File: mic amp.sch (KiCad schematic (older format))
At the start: 32 parts, among them J1 CONN_01X02, J10 CONN_01X02, J2 CONN_01X01, J3 CONN_01X03, J4 CONN_01X01, J5 CONN_01X01, J6 CONN_01X01, J7 CONN_01X01, J8 CONN_01X02, J9 CONN_01X03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

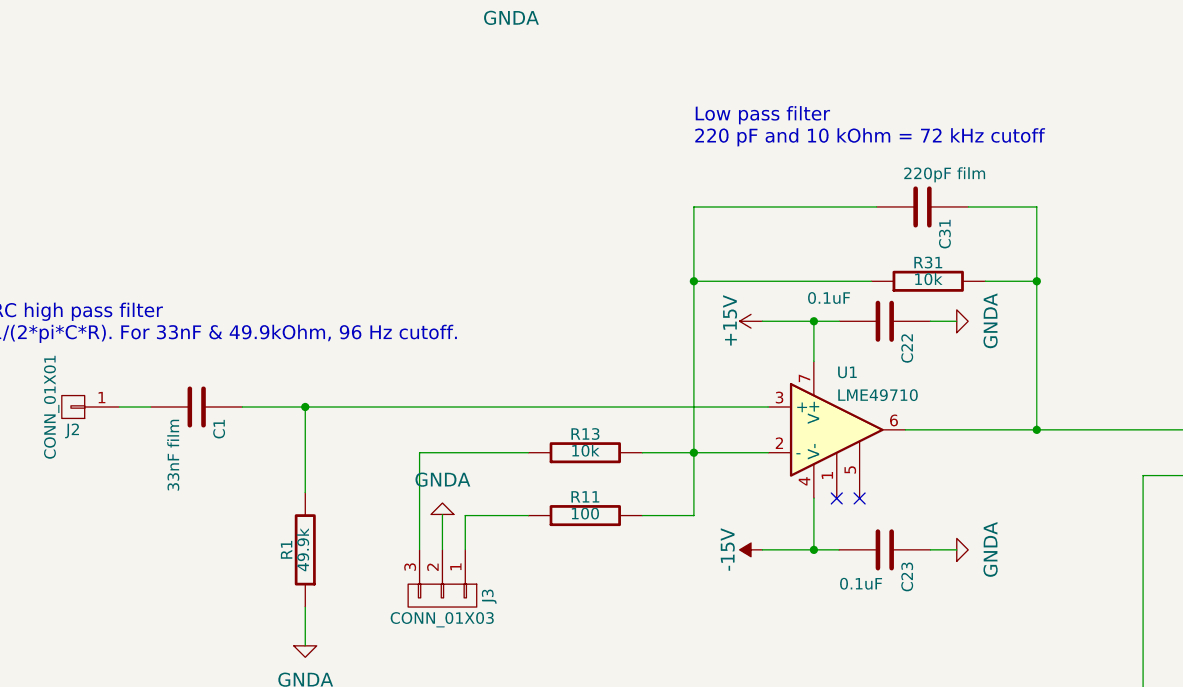
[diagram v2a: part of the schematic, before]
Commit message: Update readme and added parts list and PCB image
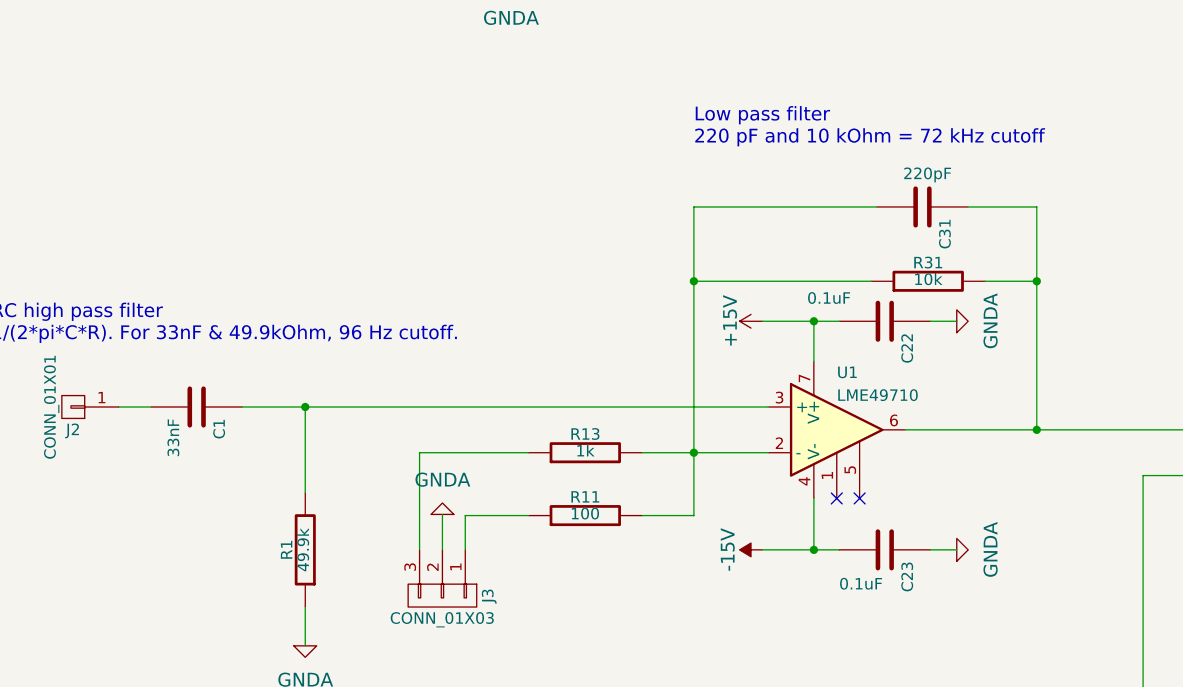
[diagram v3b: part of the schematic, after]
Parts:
- C1: value 33nF film -> 33nF; Notes (none) -> use metal film; Part number (none) -> FKP2C023301L00HI00
- C10, C11: Part number (none) -> RDER72A105K2P1H03B
- C12, C13, C22, C23, C5: Part number (none) -> RDER72A104K1S1H03A
- C31: value 220pF film -> 220pF; Notes (none) -> use metal film; Part number (none) -> FKP2D002201D00HSSD
- C6, C7: Part number (none) -> UKL1V101KPDANA
- R1: Part number (none) -> YR1B49K9CC
- R10, R11: Part number (none) -> YR1B100RCC
- R13: value 10k -> 1k; Part number (none) -> YR1B1K0CC
- R22: Part number (none) -> YR1B499RCC
- R23: Part number (none) -> YR1B90R9CC
- R24: Part number (none) -> YR1B4K75CC
- R31: Part number (none) -> YR1B10KCC
- U1: Notes (none) -> this part is end-of-life, order extra if you need more; Part number (none) -> LME49710NA/NOPB
- U2: Part number (none) -> LF356N/NOPB
- VREG1: Part number (none) -> LM317LZ/NOPB
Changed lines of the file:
@@
 F 2 "Package_TO_SOT_THT:TO-92_Inline_Wide" H 3775 1425 60  0001 C CNN
 F 3 "" H 3775 1425 60  0000 C CNN
+F 4 "LM317LZ/NOPB" H 3775 1425 60  0001 C CNN "Part number"
 	1    3775 1425
 	-1   0    0    -1
@@
 F 2 "Resistor_THT:R_Axial_DIN0207_L6.3mm_D2.5mm_P7.62mm_Horizontal" V 3705 2450 30  0001 C CNN
 F 3 "" H 3775 2450 30  0000 C CNN
+F 4 "YR1B90R9CC" H 3775 2450 60  0001 C CNN "Part number"
 	1    3775 2450
 	1    0    0    -1
@@
 F 2 "Resistor_THT:R_Axial_DIN0207_L6.3mm_D2.5mm_P7.62mm_Horizontal" V 3230 2000 30  0001 C CNN
 F 3 "" H 3300 2000 30  0000 C CNN
+F 4 "YR1B499RCC" H 3300 2000 60  0001 C CNN "Part number"
 	1    3300 2000
 	0    1    1    0
@@
 F 2 "Resistor_THT:R_Axial_DIN0207_L6.3mm_D2.5mm_P7.62mm_Horizontal" V 2405 2000 30  0001 C CNN
 F 3 "" H 2475 2000 30  0000 C CNN
+F 4 "YR1B4K75CC" H 2475 2000 60  0001 C CNN "Part number"
 	1    2475 2000
 	0    1    1    0
@@
 F 2 "custom:C_Rect_L4.0mm_W3.5mm_P2.50mm" H 4488 1875 30  0001 C CNN
 F 3 "" H 4450 2025 60  0000 C CNN
+F 4 "RDER72A104K1S1H03A" H 4450 2025 60  0001 C CNN "Part number"
 	1    4450 2025
 	1    0    0    -1
@@
 F 2 "Capacitor_THT:CP_Radial_D10.0mm_P5.00mm" H 2938 2300 30  0001 C CNN
 F 3 "" H 2900 2450 60  0000 C CNN
+F 4 "UKL1V101KPDANA" H 2900 2450 60  0001 C CNN "Part number"
 	1    2900 2450
 	1    0    0    -1
@@
 F 2 "Capacitor_THT:CP_Radial_D10.0mm_P5.00mm" H 2088 2300 30  0001 C CNN
 F 3 "" H 2050 2450 60  0000 C CNN
+F 4 "UKL1V101KPDANA" H 2050 2450 60  0001 C CNN "Part number"
 	1    2050 2450
 	1    0    0    -1
@@
 F 2 "Resistor_THT:R_Axial_DIN0207_L6.3mm_D2.5mm_P7.62mm_Horizontal" V 2380 5675 30  0001 C CNN
 F 3 "" H 2450 5675 30  0000 C CNN
+F 4 "YR1B49K9CC" H 2450 5675 60  0001 C CNN "Part number"
 	1    2450 5675
 	-1   0    0    1
@@
 P 1975 5050
 F 0 "C1" H 2025 5150 50  0000 L CNN
-F 1 "33nF film" H 2025 4950 50  0000 L CNN
+F 1 "33nF" H 2025 4950 50  0000 L CNN
 F 2 "Capacitor_THT:C_Rect_L7.2mm_W8.5mm_P5.00mm_FKP2_FKP2_MKS2_MKP2" H 2013 4900 30  0001 C CNN
 F 3 "" H 1975 5050 60  0000 C CNN
+F 4 "FKP2C023301L00HI00" H 1975 5050 60  0001 C CNN "Part number"
+F 5 "use metal film" H 1975 5050 60  0001 C CNN "Notes"
 	1    1975 5050
 	0    1    1    0
@@
 P 3675 5250
 F 0 "R13" V 3755 5250 50  0000 C CNN
-F 1 "10k" V 3682 5251 50  0000 C CNN
+F 1 "1k" V 3682 5251 50  0000 C CNN
 F 2 "Resistor_THT:R_Axial_DIN0207_L6.3mm_D2.5mm_P7.62mm_Horizontal" V 3605 5250 30  0001 C CNN
 F 3 "" H 3675 5250 30  0000 C CNN
+F 4 "YR1B1K0CC" H 3675 5250 60  0001 C CNN "Part number"
 	1    3675 5250
 	0    -1   -1   0
@@
 F 2 "Resistor_THT:R_Axial_DIN0207_L6.3mm_D2.5mm_P7.62mm_Horizontal" V 3605 5525 30  0001 C CNN
 F 3 "" H 3675 5525 30  0000 C CNN
+F 4 "YR1B100RCC" H 3675 5525 60  0001 C CNN "Part number"
 	1    3675 5525
 	0    -1   -1   0
@@
 F 2 "Resistor_THT:R_Axial_DIN0207_L6.3mm_D2.5mm_P7.62mm_Horizontal" V 5105 4500 30  0001 C CNN
 F 3 "" H 5175 4500 30  0000 C CNN
+F 4 "YR1B10KCC" H 5175 4500 60  0001 C CNN "Part number"
 	1    5175 4500
 	0    -1   -1   0
@@
 P 5150 4175
 F 0 "C31" H 5200 4275 50  0000 L CNN
-F 1 "220pF film" V 5005 4090 50  0000 L CNN
+F 1 "220pF" V 5005 4090 50  0000 L CNN
 F 2 "Capacitor_THT:C_Rect_L7.2mm_W4.5mm_P5.00mm_FKS2_FKP2_MKS2_MKP2" H 5188 4025 30  0001 C CNN
 F 3 "" H 5150 4175 60  0000 C CNN
+F 4 "FKP2D002201D00HSSD" H 5150 4175 60  0001 C CNN "Part number"
+F 5 "use metal film" H 5150 4175 60  0001 C CNN "Notes"
 	1    5150 4175
 	0    1    1    0
@@
 F 2 "custom:C_Rect_L4.0mm_W3.5mm_P2.50mm" H 7088 4600 30  0001 C CNN
 F 3 "" H 7050 4750 60  0000 C CNN
+F 4 "RDER72A104K1S1H03A" H 7050 4750 60  0001 C CNN "Part number"
 	1    7050 4750
 	0    1    1    0
@@
 F 2 "custom:C_Rect_L4.0mm_W3.5mm_P2.50mm" H 7088 5600 30  0001 C CNN
 F 3 "" H 7050 5750 60  0000 C CNN
+F 4 "RDER72A104K1S1H03A" H 7050 5750 60  0001 C CNN "Part number"
 	1    7050 5750
 	0    1    1    0
@@
 F 2 "Resistor_THT:R_Axial_DIN0207_L6.3mm_D2.5mm_P7.62mm_Horizontal" V 7730 5250 30  0001 C CNN
 F 3 "" H 7800 5250 30  0000 C CNN
+F 4 "YR1B100RCC" H 7800 5250 60  0001 C CNN "Part number"
 	1    7800 5250
 	0    -1   -1   0
@@
 F 2 "custom:C_Rect_L5.5mm_W4.0mm_P2.50mm" H 6418 2300 30  0001 C CNN
 F 3 "" H 6380 2450 60  0000 C CNN
+F 4 "RDER72A105K2P1H03B" H 6380 2450 60  0001 C CNN "Part number"
 	1    6380 2450
 	1    0    0    -1
@@
 F 2 "custom:C_Rect_L5.5mm_W4.0mm_P2.50mm" H 6088 2300 30  0001 C CNN
 F 3 "" H 6050 2450 60  0000 C CNN
+F 4 "RDER72A105K2P1H03B" H 6050 2450 60  0001 C CNN "Part number"
 	1    6050 2450
 	1    0    0    -1
@@
 F 2 "custom:C_Rect_L4.0mm_W3.5mm_P2.50mm" H 5023 4525 30  0001 C CNN
 F 3 "" H 4985 4675 60  0000 C CNN
+F 4 "RDER72A104K1S1H03A" H 4985 4675 60  0001 C CNN "Part number"
 	1    4985 4675
 	0    1    1    0
@@
 F 2 "custom:C_Rect_L4.0mm_W3.5mm_P2.50mm" H 5023 5525 30  0001 C CNN
 F 3 "" H 4985 5675 60  0000 C CNN
+F 4 "RDER72A104K1S1H03A" H 4985 5675 60  0001 C CNN "Part number"
 	1    4985 5675
 	0    1    1    0
@@
 F 2 "Package_DIP:DIP-8_W7.62mm_LongPads" H 6745 5300 50  0001 C CNN
 F 3 "" H 6845 5400 50  0001 C CNN
+F 4 "LF356N/NOPB" H 6695 5250 60  0001 C CNN "Part number"
 	1    6695 5250
 	1    0    0    -1
@@
 F 2 "Package_DIP:DIP-8_W7.62mm_LongPads" H 4825 5200 50  0001 C CNN
 F 3 "" H 4925 5300 50  0001 C CNN
+F 4 "LME49710NA/NOPB" H 4775 5150 60  0001 C CNN "Part number"
+F 5 "this part is end-of-life, order extra if you need more" H 4775 5150 60  0001 C CNN "Notes"
 	1    4775 5150
 	1    0    0    -1

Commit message: Update parts list, fix circuit board image
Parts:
- J1, J10, J2, J3, J8, J9: Notes (none) -> 0.1\" header
- J4, J5, J6, J7: Notes (none) -> mounting hole
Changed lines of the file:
@@
 F 2 "Conn_PinSocket_2.54mm:PinSocket_1x03_P2.54mm_Vertical" H 3050 5875 50  0001 C CNN
 F 3 "" H 3050 5875 50  0001 C CNN
+F 4 "0.1\" header" H 3050 5875 60  0001 C CNN "Notes"
 	1    3050 5875
 	0    1    1    0
@@
 F 2 "MountingHole:MountingHole_3.2mm_M3" H 8985 1805 50  0001 C CNN
 F 3 "" H 8985 1805 50  0001 C CNN
+F 4 "mounting hole" H 8985 1805 60  0001 C CNN "Notes"
 	1    8985 1805
 	1    0    0    -1
@@
 F 2 "MountingHole:MountingHole_3.2mm_M3" H 8995 2180 50  0001 C CNN
 F 3 "" H 8995 2180 50  0001 C CNN
+F 4 "mounting hole" H 8995 2180 60  0001 C CNN "Notes"
 	1    8995 2180
 	1    0    0    -1
@@
 F 2 "MountingHole:MountingHole_3.2mm_M3" H 8980 2595 50  0001 C CNN
 F 3 "" H 8980 2595 50  0001 C CNN
+F 4 "mounting hole" H 8980 2595 60  0001 C CNN "Notes"
 	1    8980 2595
 	1    0    0    -1
@@
 F 2 "MountingHole:MountingHole_3.2mm_M3" H 8935 1415 50  0001 C CNN
 F 3 "" H 8935 1415 50  0001 C CNN
+F 4 "mounting hole" H 8935 1415 60  0001 C CNN "Notes"
 	1    8935 1415
 	1    0    0    -1
@@
 F 2 "Conn_PinSocket_2.54mm:PinSocket_1x02_P2.54mm_Vertical" H 8725 5200 50  0001 C CNN
 F 3 "" H 8725 5200 50  0001 C CNN
+F 4 "0.1\" header" H 8725 5200 60  0001 C CNN "Notes"
 	1    8725 5200
 	1    0    0    -1
@@
 F 2 "Conn_PinSocket_2.54mm:PinSocket_1x02_P2.54mm_Vertical" H 1150 2050 50  0001 C CNN
 F 3 "" H 1150 2050 50  0001 C CNN
+F 4 "0.1\" header" H 1150 2050 60  0001 C CNN "Notes"
 	1    1150 2050
 	-1   0    0    1
@@
 F 2 "Conn_PinSocket_2.54mm:PinSocket_1x01_P2.54mm_Vertical" H 1435 5050 50  0001 C CNN
 F 3 "" H 1435 5050 50  0001 C CNN
+F 4 "0.1\" header" H 1435 5050 60  0001 C CNN "Notes"
 	1    1435 5050
 	-1   0    0    1
@@
 F 2 "Conn_PinSocket_2.54mm:PinSocket_1x03_P2.54mm_Vertical" H 6655 1035 50  0001 C CNN
 F 3 "" H 6655 1035 50  0001 C CNN
+F 4 "0.1\" header" H 6655 1035 60  0001 C CNN "Notes"
 	1    6655 1035
 	-1   0    0    1
@@
 F 2 "Conn_PinSocket_2.54mm:PinSocket_1x02_P2.54mm_Vertical" H 6980 1530 50  0001 C CNN
 F 3 "" H 6980 1530 50  0001 C CNN
+F 4 "0.1\" header" H 6980 1530 60  0001 C CNN "Notes"
 	1    6980 1530
 	-1   0    0    1
